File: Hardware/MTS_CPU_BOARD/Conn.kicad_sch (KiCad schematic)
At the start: 8 parts, among them J1 DIN41612_02x16_ZB, SW1 SW_DIP_x04, U1 TCAN337GDR, U3 24LC32

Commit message: Add some connectors
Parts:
- added J3: HDMI_A_1.4, Connector_Video:HDMI_A_Kycon_KDMIX-SL1-NS-WS-B15_VerticalRightAngle, symbol Connector:HDMI_A_1.4
- added J4: USB3_A_Stacked, Connector_USB:USB3_A_Molex_48406-0001_Horizontal_Stacked, symbol Connector:USB3_A_Stacked
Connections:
- new net: J4.1 (VBUS1), J4.10 (VBUS2)
- new net: J4.19 (SHIELD), J4.19 (SHIELD)
- new net: J4.11 (D2-), J4.2 (D1-)
- new net: J4.12 (D2+), J4.3 (D1+)
- new net: J4.13 (GND2), J4.4 (GND1)
- new net: J4.14 (SSRX2-), J4.5 (SSRX1-)
- new net: J4.15 (SSRX2+), J4.6 (SSRX1+)
- new net: J4.16 (DRAIN2), J4.7 (DRAIN1)
- new net: J4.17 (SSTX2-), J4.8 (SSTX1-)
- new net: J4.18 (SSTX2+), J4.9 (SSTX1+)

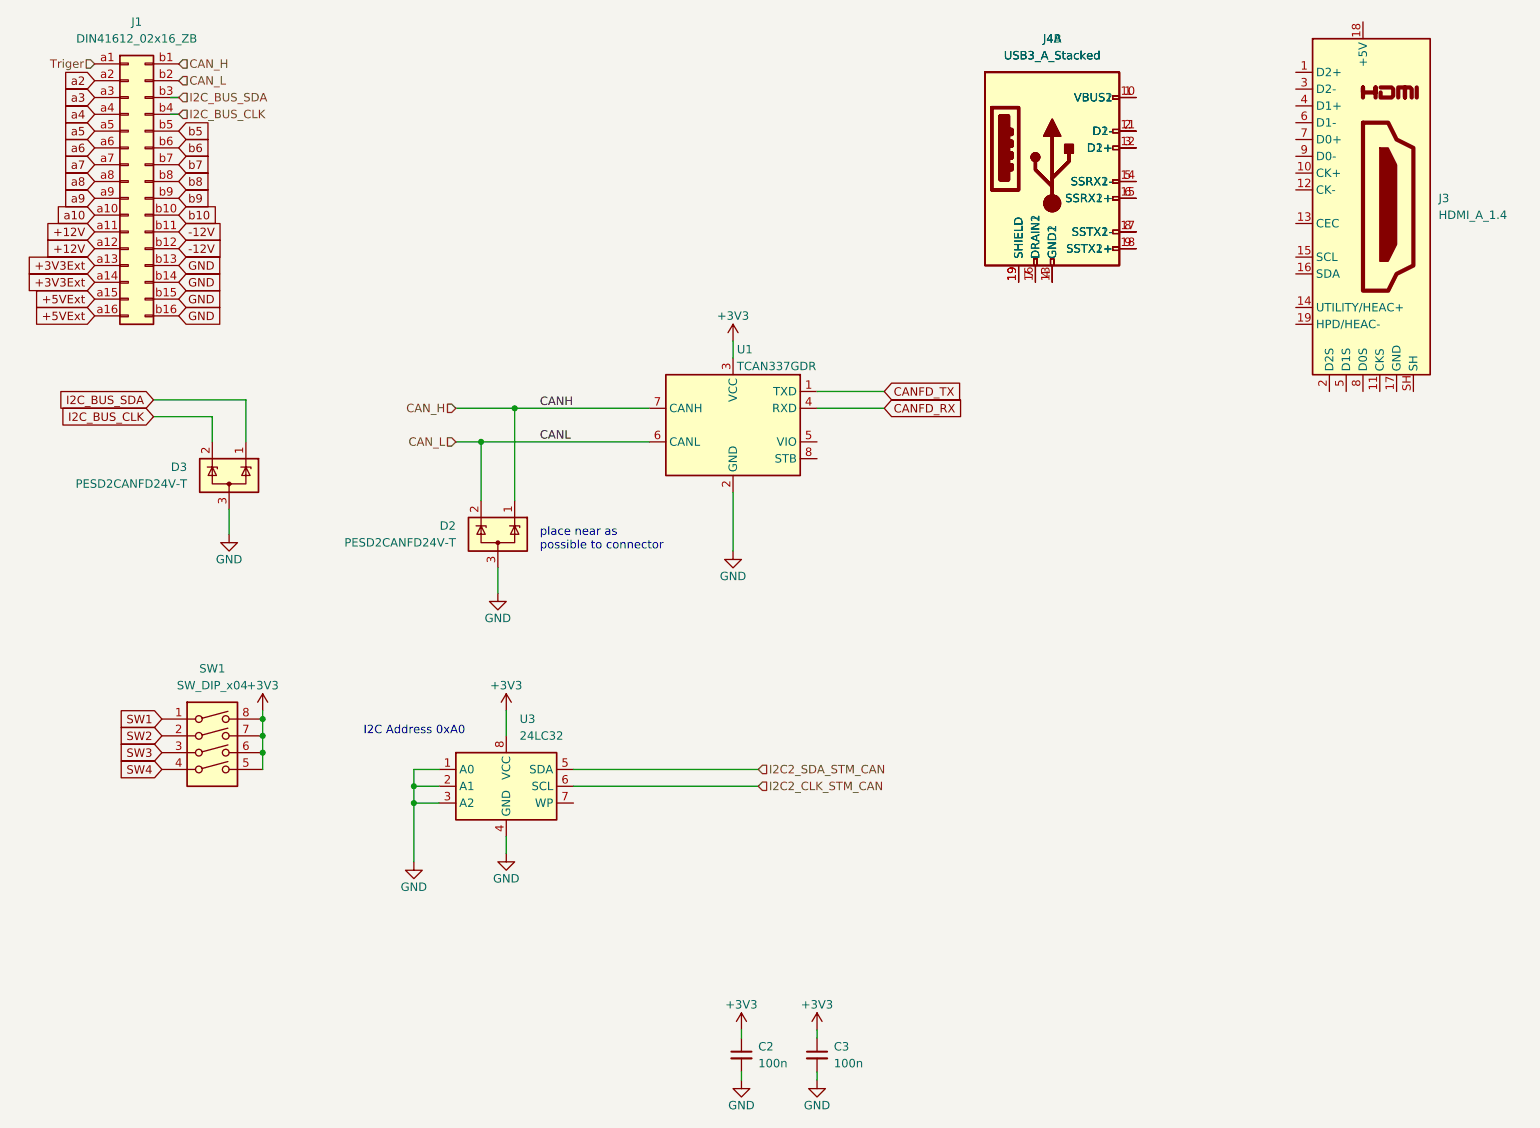
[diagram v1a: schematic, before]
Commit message: Add EtherCAT
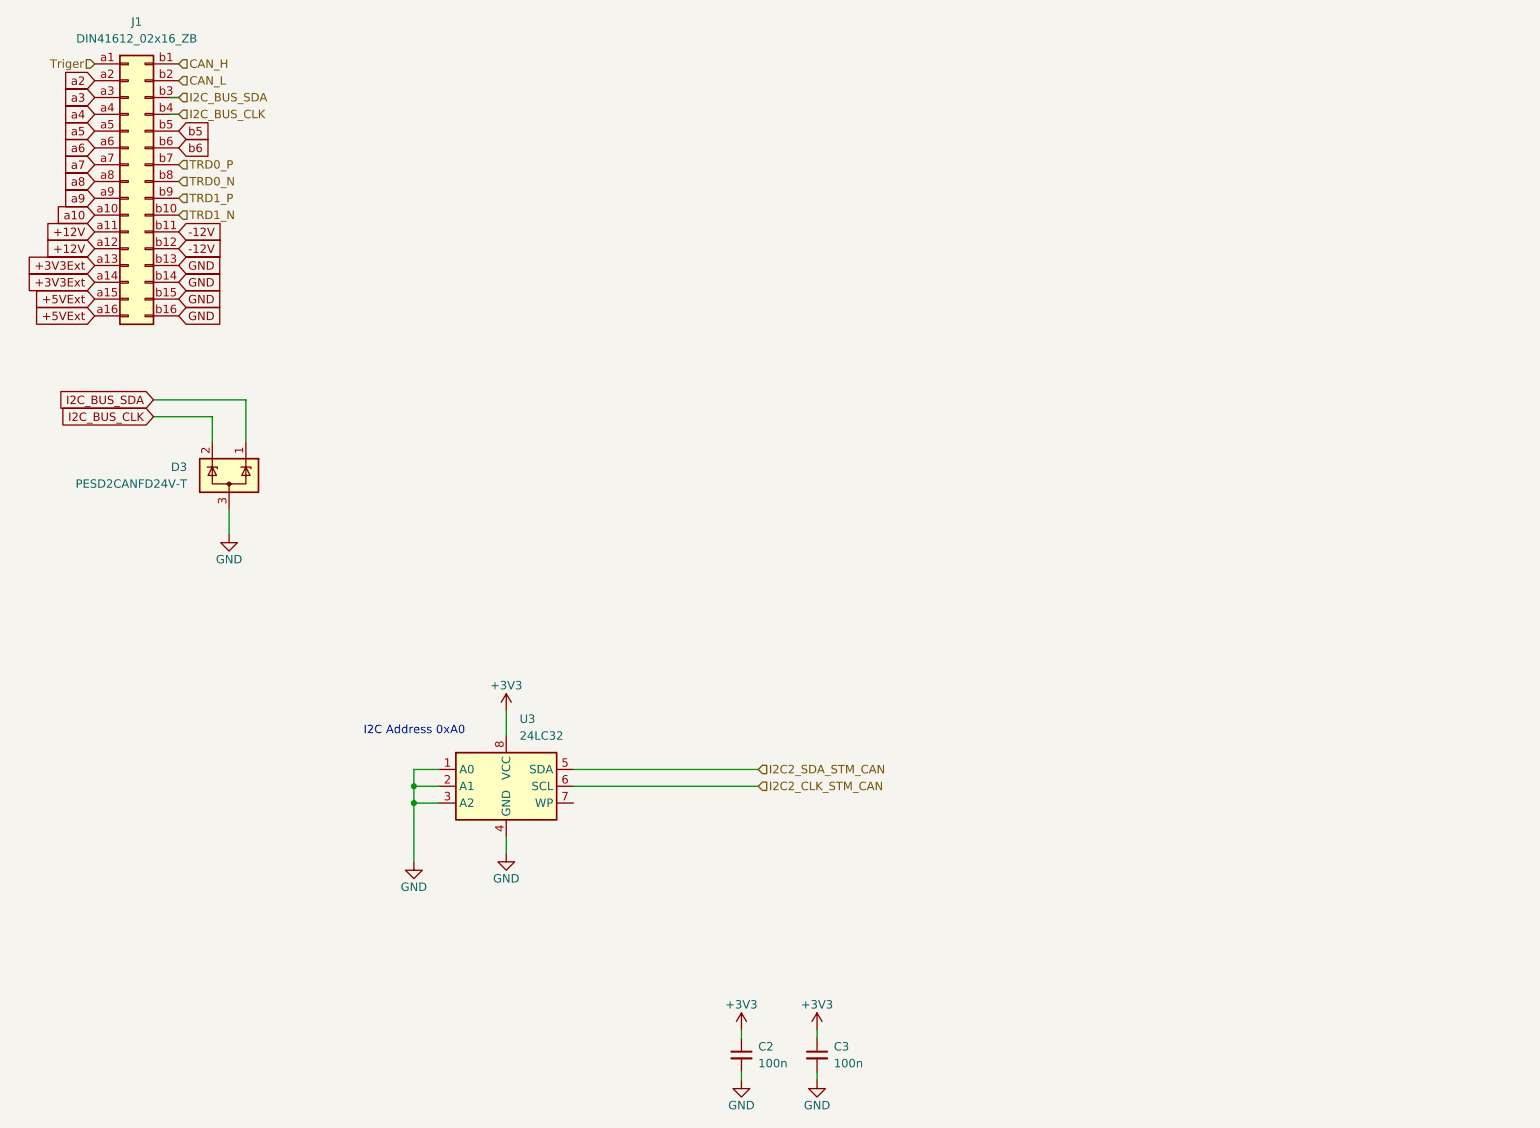
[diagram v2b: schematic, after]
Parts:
- removed D2: PESD2CANFD24V-T, Package_TO_SOT_SMD:SOT-23, symbol Power_Protection:SP0502BAHT
- removed J3: HDMI_A_1.4, Connector_Video:HDMI_A_Kycon_KDMIX-SL1-NS-WS-B15_VerticalRightAngle, symbol Connector:HDMI_A_1.4
- removed J4: USB3_A_Stacked, Connector_USB:USB3_A_Molex_48406-0001_Horizontal_Stacked, symbol Connector:USB3_A_Stacked
- removed SW1: SW_DIP_x04, Button_Switch_SMD:SW_DIP_SPSTx04_Slide_6.7x11.72mm_W8.61mm_P2.54mm_LowProfile, symbol Switch:SW_DIP_x04
- removed U1: TCAN337GDR, Package_SO:SOIC-8_3.9x4.9mm_P1.27mm, symbol Interface_CAN_LIN:TJA1042T-3
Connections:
- net b10 renamed TRD1_N
- net b7 renamed TRD0_P
- net b8 renamed TRD0_N
- net b9 renamed TRD1_P
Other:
- note removed: "place near as possible to connector"

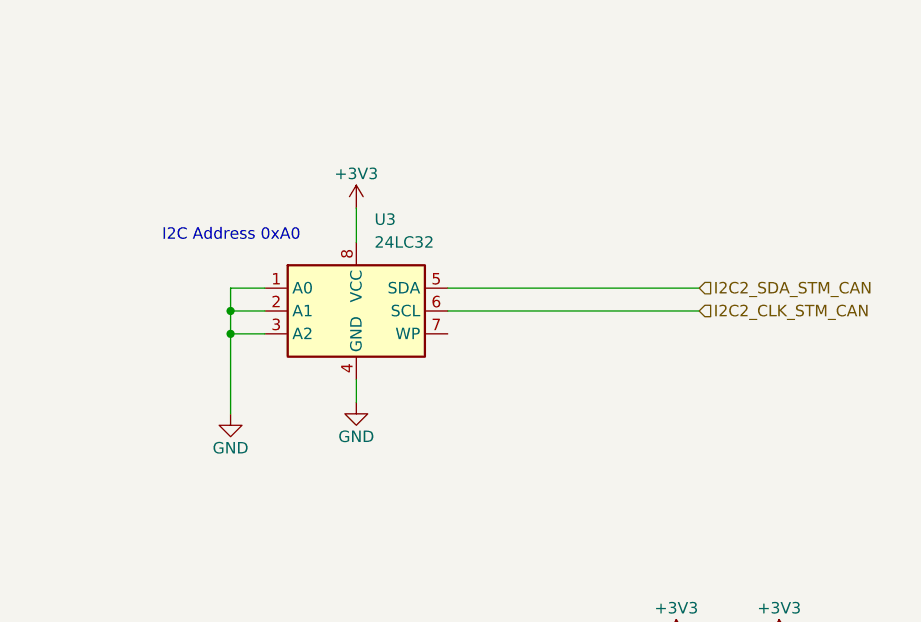
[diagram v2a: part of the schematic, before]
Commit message: Add status Led´s
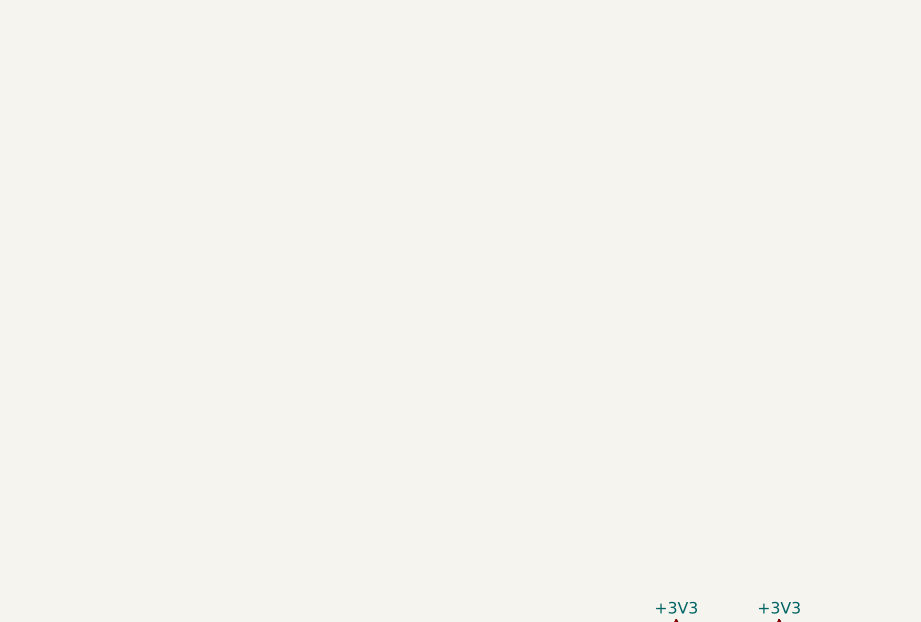
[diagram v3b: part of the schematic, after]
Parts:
- removed U3: 24LC32, Package_SO:SOIC-8_3.9x4.9mm_P1.27mm, symbol Memory_EEPROM:24LC32
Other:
- note removed: "I2C Address 0xA0"
